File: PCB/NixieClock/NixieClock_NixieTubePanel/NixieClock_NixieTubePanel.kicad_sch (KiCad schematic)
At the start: 30 parts, among them J3 Conn_01x04_Pin, J4 Conn_01x04_Pin, U1 K155ID1, U2 K155ID1, U3 K155ID1, U4 K155ID1, U5 PCF8574, U6 PCF8574, X1 5230, X2 5230, X3 5230, X4 5230, X5 5230, X6 5230

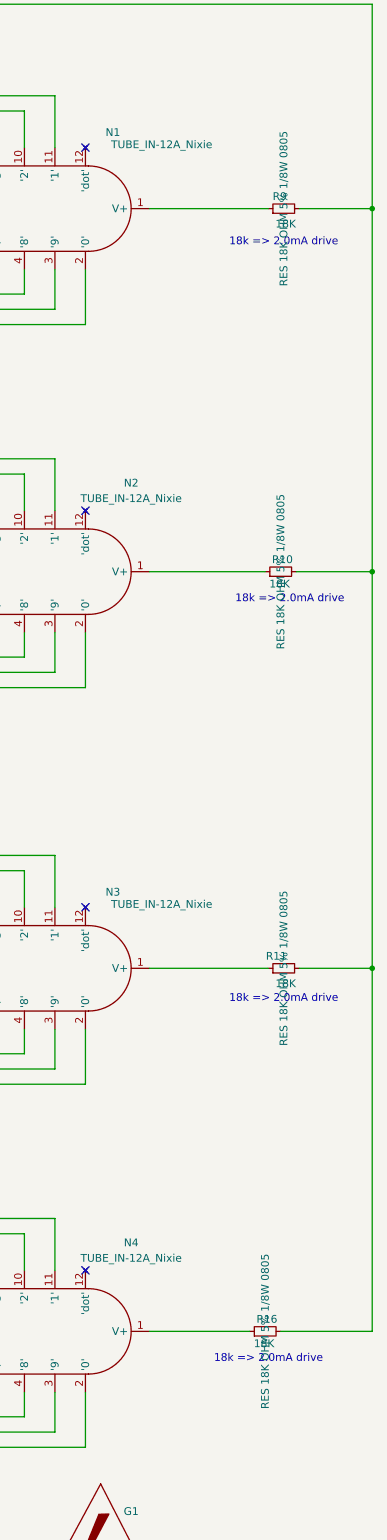
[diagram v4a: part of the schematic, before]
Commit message: Correct part details from 0805 to 1206 missed in previous commit
also correct BOM
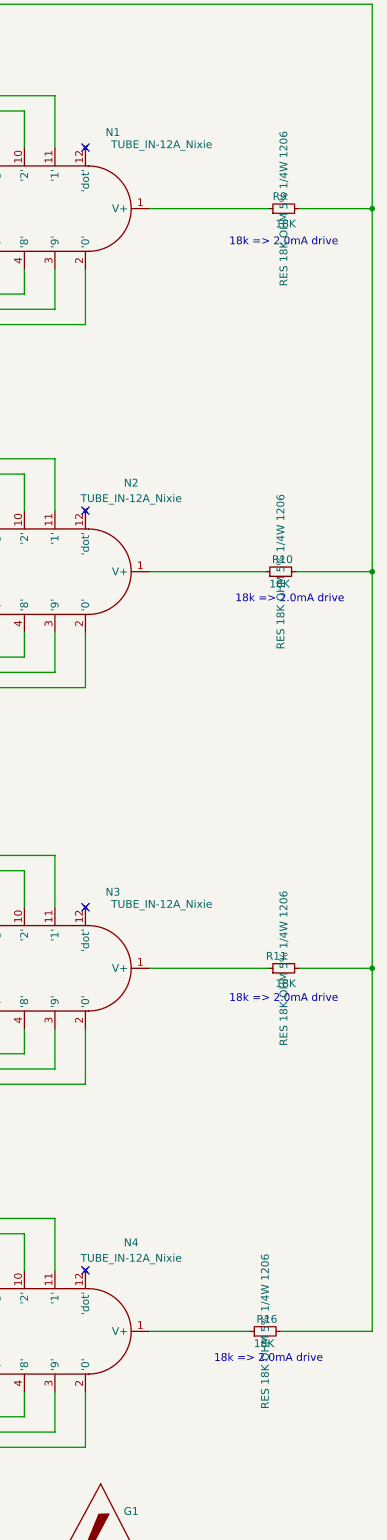
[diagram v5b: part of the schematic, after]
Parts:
- R10, R11, R16, R9: Manufacturer PN RC0805JR-0718KL -> RC1206JR-0718KL
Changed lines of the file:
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@@
 			)
 		)
-		(property "Description" "RES 18K OHM 5% 1/8W 0805"
+		(property "Description" "RES 18K OHM 5% 1/4W 1206"
 			(at 294.46 237.5 0)
 			(effects
@@
 			)
 		)
-		(property "Manufacturer PN" "RC0805JR-0718KL"
+		(property "Manufacturer PN" "RC1206JR-0718KL"
 			(at 294.46 237.5 90)
 			(effects
@@
 			)
 		)
-		(property "Description" "RES 18K OHM 5% 1/8W 0805"
+		(property "Description" "RES 18K OHM 5% 1/4W 1206"
 			(at 297.5 178 0)
 			(effects
@@
 			)
 		)
-		(property "Manufacturer PN" "RC0805JR-0718KL"
+		(property "Manufacturer PN" "RC1206JR-0718KL"
 			(at 297.5 178 90)
 			(effects
@@
 			)
 		)
-		(property "Description" "RES 18K OHM 5% 1/8W 0805"
+		(property "Description" "RES 18K OHM 5% 1/4W 1206"
 			(at 297.5 53.5 0)
 			(effects
@@
 			)
 		)
-		(property "Manufacturer PN" "RC0805JR-0718KL"
+		(property "Manufacturer PN" "RC1206JR-0718KL"
 			(at 297.5 53.5 90)
 			(effects
@@
 			)
 		)
-		(property "Description" "RES 18K OHM 5% 1/8W 0805"
+		(property "Description" "RES 18K OHM 5% 1/4W 1206"
 			(at 297 113 0)
 			(effects
@@
 			)
 		)
-		(property "Manufacturer PN" "RC0805JR-0718KL"
+		(property "Manufacturer PN" "RC1206JR-0718KL"
 			(at 297 113 90)
 			(effects

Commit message: decoupling caps 0603 -> 0805 for easier soldering
prototype feedback found that decoupling caps can be 0805 sized and easier to hand solder. 0603 is not required
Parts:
- C10, C5, C6, C7, C8, C9: footprint Capacitor_SMD:C_0603_1608Metric_Pad1.08x0.95mm_HandSolder -> Capacitor_SMD:C_0805_2012Metric_Pad1.18x1.45mm_HandSolder
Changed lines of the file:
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@@
 			)
 		)
-		(property "Footprint" "Capacitor_SMD:C_0603_1608Metric_Pad1.08x0.95mm_HandSolder"
+		(property "Footprint" "Capacitor_SMD:C_0805_2012Metric_Pad1.18x1.45mm_HandSolder"
 			(at 178 33.5 0)
 			(effects
@@
 			)
 		)
-		(property "Footprint" "Capacitor_SMD:C_0603_1608Metric_Pad1.08x0.95mm_HandSolder"
+		(property "Footprint" "Capacitor_SMD:C_0805_2012Metric_Pad1.18x1.45mm_HandSolder"
 			(at 129.5 181 0)
 			(effects
@@
 			)
 		)
-		(property "Footprint" "Capacitor_SMD:C_0603_1608Metric_Pad1.08x0.95mm_HandSolder"
+		(property "Footprint" "Capacitor_SMD:C_0805_2012Metric_Pad1.18x1.45mm_HandSolder"
 			(at 178 158 0)
 			(effects
@@
 			)
 		)
-		(property "Footprint" "Capacitor_SMD:C_0603_1608Metric_Pad1.08x0.95mm_HandSolder"
+		(property "Footprint" "Capacitor_SMD:C_0805_2012Metric_Pad1.18x1.45mm_HandSolder"
 			(at 176 130.5 0)
 			(effects
@@
 			)
 		)
-		(property "Footprint" "Capacitor_SMD:C_0603_1608Metric_Pad1.08x0.95mm_HandSolder"
+		(property "Footprint" "Capacitor_SMD:C_0805_2012Metric_Pad1.18x1.45mm_HandSolder"
 			(at 174.5 259 0)
 			(effects
@@
 			)
 		)
-		(property "Footprint" "Capacitor_SMD:C_0603_1608Metric_Pad1.08x0.95mm_HandSolder"
+		(property "Footprint" "Capacitor_SMD:C_0805_2012Metric_Pad1.18x1.45mm_HandSolder"
 			(at 129.5 56.5 0)
 			(effects

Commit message: component manufacturer details were incorrect
deleted "MANUFACTURER" and "MANUFACTURER P/N" fields. now using "Manufacturer" "Manufacturer PN" consistently across project
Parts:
- U2, U3, U4: MANUFACTURER MSI -> (none)
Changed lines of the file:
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@@
 			)
 		)
-		(property "MANUFACTURER" "MSI"
-			(at 139.4 131.5 0)
-			(effects
-				(font
-					(size 1.27 1.27)
-				)
-				(justify bottom)
-				(hide yes)
-			)
-		)
 		(property "Checked" ""
 			(at 183 131.5 0)
@@
 			)
 		)
-		(property "Manufacturer P/N" ""
-			(at 183 131.5 0)
-			(effects
-				(font
-					(size 1.27 1.27)
-				)
-				(hide yes)
-			)
-		)
 		(property "Manufacturer PN" "Unknown"
 			(at 183 131.5 0)
@@
 			)
 		)
-		(property "MANUFACTURER" "MSI"
-			(at 139.4 256 0)
-			(effects
-				(font
-					(size 1.27 1.27)
-				)
-				(justify bottom)
-				(hide yes)
-			)
-		)
 		(property "Checked" ""
 			(at 183 256 0)
@@
 			)
 		)
-		(property "Manufacturer P/N" ""
-			(at 183 256 0)
-			(effects
-				(font
-					(size 1.27 1.27)
-				)
-				(hide yes)
-			)
-		)
 		(property "Manufacturer PN" "Unknown"
 			(at 183 256 0)
@@
 			)
 		)
-		(property "MANUFACTURER" "MSI"
-			(at 139.4 196.5 0)
-			(effects
-				(font
-					(size 1.27 1.27)
-				)
-				(justify bottom)
-				(hide yes)
-			)
-		)
 		(property "Checked" ""
 			(at 183 196.5 0)
@@
 			)
 		)
-		(property "Manufacturer P/N" ""
-			(at 183 196.5 0)
-			(effects
-				(font
-					(size 1.27 1.27)
-				)
-				(hide yes)
-			)
-		)
 		(property "Manufacturer PN" "Unknown"
 			(at 183 196.5 0)
@@
 			)
 		)
-		(property "Manufacturer P/N" ""
-			(at 183 72 0)
-			(effects
-				(font
-					(size 1.27 1.27)
-				)
-				(hide yes)
-			)
-		)
